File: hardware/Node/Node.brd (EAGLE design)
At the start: 49.5 x 49.5 mm, 71 parts, among them J1 AVR_SPI_PRG_6NS, J2 M04X2, Q1 PMR280UN, Q2 PMR280UN, Q3 PMR280UN, SW1 KSS, SW2 KSS, U1 ATMEGA32U4QFN, U2 BLUETOOTH-RN41", U3 LSM303DLM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

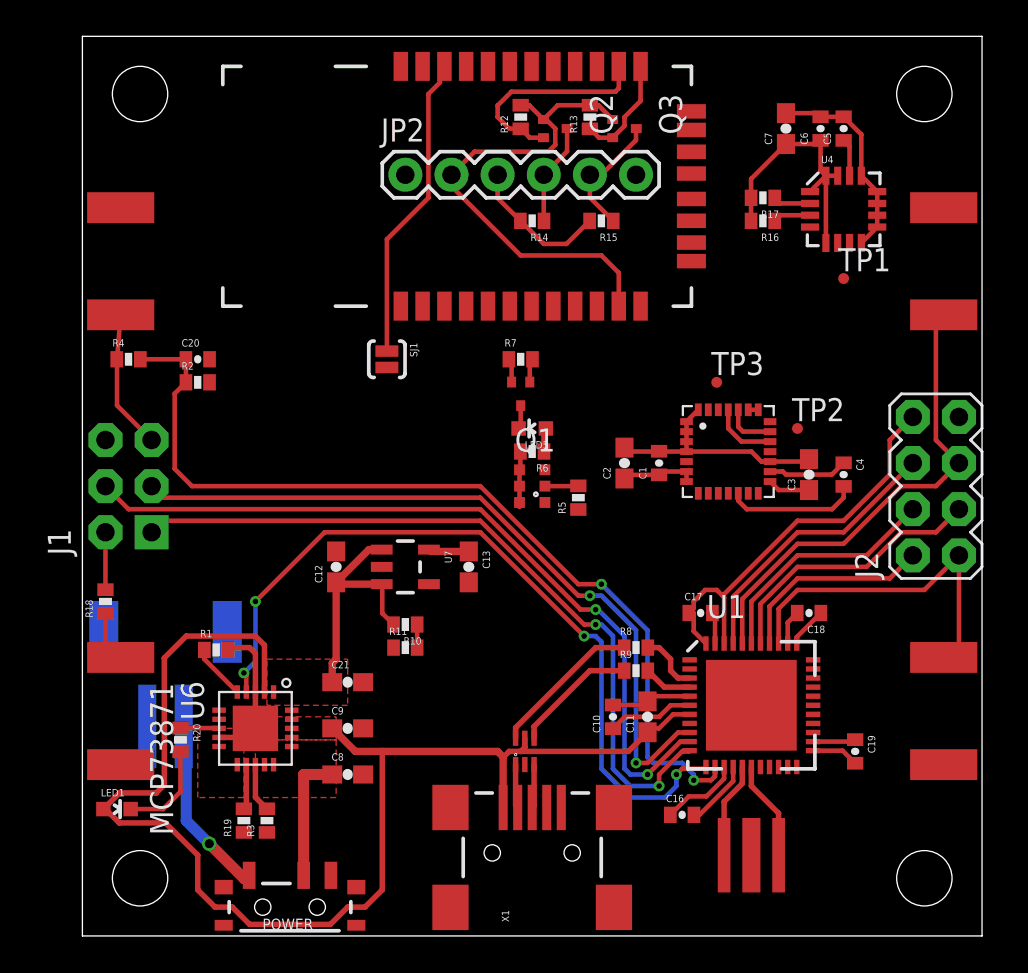
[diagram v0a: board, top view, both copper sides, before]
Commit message: route LEDs and interrupts
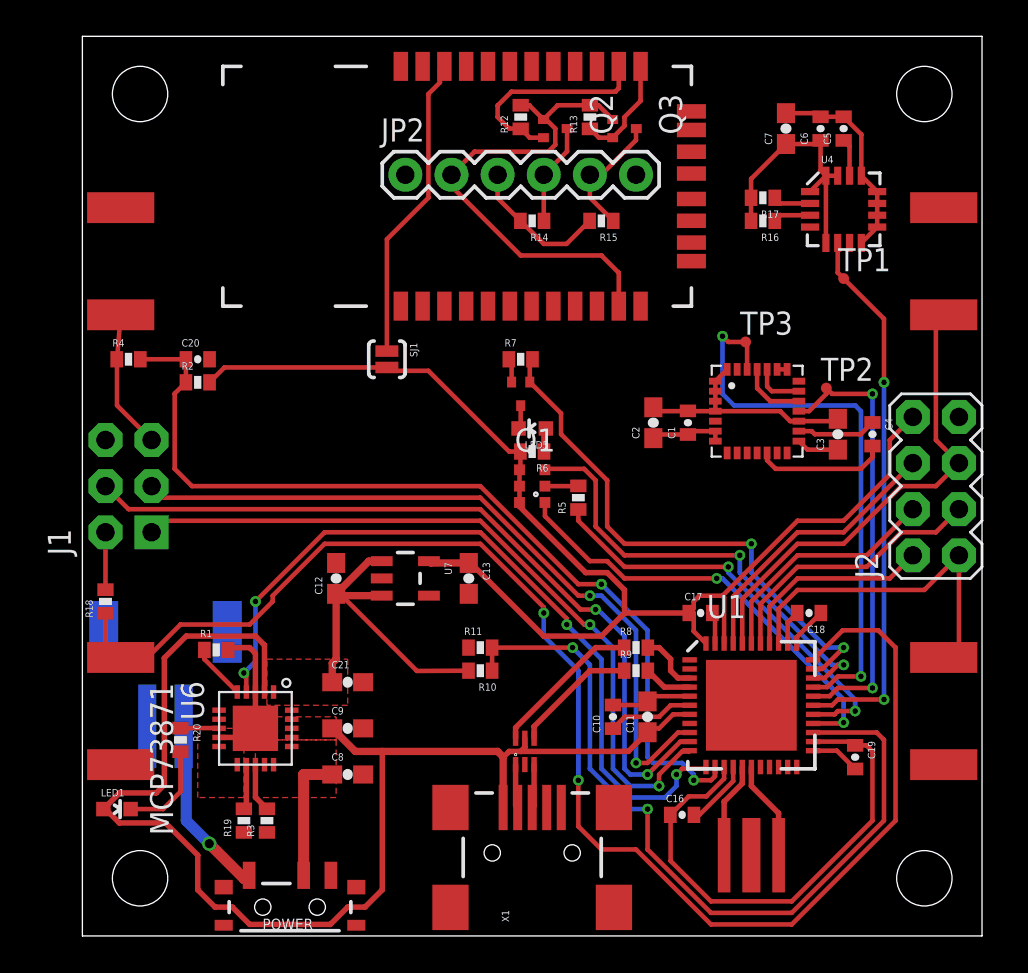
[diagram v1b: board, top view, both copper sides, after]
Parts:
- moved R10 4.85 mm to (21.9, 14.6)
- moved R11 4.13 mm to (21.9, 15.9)
- moved C4 2.73 mm to (43.5, 27.6)
- moved TP2 2.73 mm to (41.0, 30.2)
- moved TP3 2.73 mm to (36.5, 32.7)
- moved C2 2.73 mm to (31.4, 28.3)
- moved C1 2.73 mm to (33.3, 28.3)
- moved C3 2.73 mm to (41.6, 27.6)
- moved U3 2.73 mm to (37.1, 28.9)
- moved C12 0.64 mm to (14.0, 19.7)
- moved C13 0.64 mm to (21.3, 19.7)
- moved U7 0.64 mm to (17.8, 19.7)
- moved C19 0.32 mm to (42.5, 9.84)
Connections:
- net N$12: now also LED4.3; no longer LED4.1
- net N$17: now also LED4.1, U1.26; no longer LED4.3, U1.32
- net N$22: now also U1.32; no longer U1.26
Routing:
- net HWB: track 2.79 -> 80.4 mm, vias 0 -> 2
- net +3V3: track 92.7 -> 156.3 mm
- net VDIV: track 1.27 -> 44.2 mm, vias 0 -> 2
- net PCINT6: track 0.00 -> 31.6 mm, vias 0 -> 2
- net PCINT4: track 0.00 -> 30.2 mm, vias 0 -> 2
- net N$22: track 1.32 -> 29.9 mm, vias 0 -> 2
- net N$12: track 0.00 -> 24.7 mm, vias 0 -> 2
- net PCINT5: track 0.00 -> 24.5 mm, vias 0 -> 2
- net N$17: track 0.00 -> 24.3 mm, vias 0 -> 2
- net N$18: track 0.00 -> 23.1 mm, vias 0 -> 2
- net N$11: track 13.6 -> 19.9 mm

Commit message: lay ground pours
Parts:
- moved C5 2.22 mm to (41.9, 42.2)
- moved C6 2.22 mm to (40.6, 42.2)
- moved C7 2.22 mm to (38.7, 42.2)
- moved R17 2.22 mm to (37.5, 38.4)
- moved TP1 2.22 mm to (41.9, 34.0)
- moved U4 2.22 mm to (41.9, 37.8)
- moved R16 2.22 mm to (37.5, 37.1)
- moved TP2 0.63 mm to (41.6, 30.2)
- moved TP3 0.32 mm to (36.2, 32.7)
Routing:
- net +3V3: track 156.3 -> 233.0 mm, vias 0 -> 8
- net RX: track 11.9 -> 69.3 mm, vias 0 -> 2
- net TX: track 6.02 -> 60.3 mm, vias 0 -> 2
- net SCL: track 4.89 -> 55.4 mm, vias 0 -> 2
- net SDA: track 5.70 -> 53.2 mm, vias 0 -> 2
- net RBT: track 0.00 -> 46.1 mm, vias 0 -> 2
- net SBT: track 0.00 -> 37.8 mm, vias 0 -> 4
- net VBUS: track 72.0 -> 100.8 mm, vias 0 -> 2
- net GND: track 48.8 -> 44.6 mm
- net N$17: track 24.3 -> 28.2 mm
- net N$11: track 19.9 -> 18.2 mm
- net PROG2: track 42.5 -> 43.8 mm
- net PCINT4: track 30.2 -> 29.3 mm
- net N$18: track 23.1 -> 24.0 mm
- net MISO: track 41.0 -> 41.5 mm
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- added copper zone on layer 16, net GND

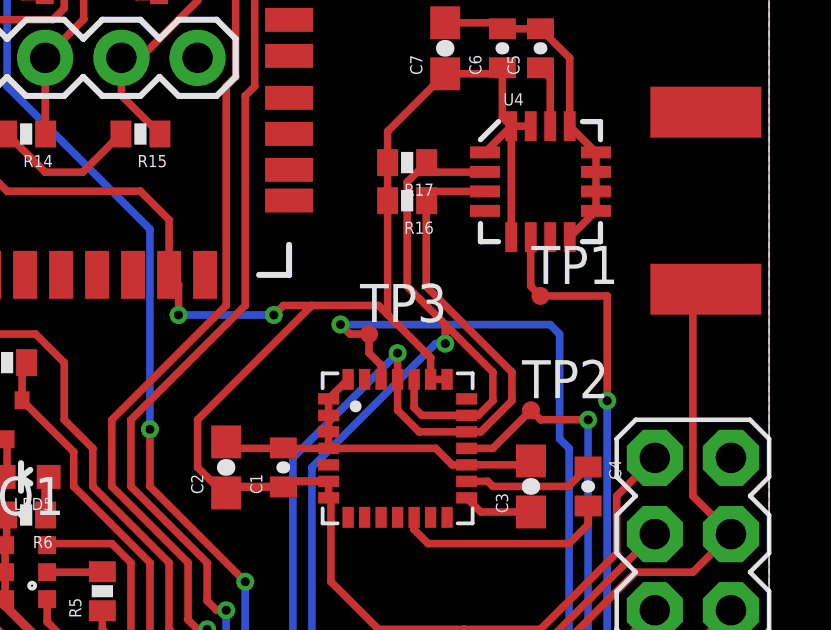
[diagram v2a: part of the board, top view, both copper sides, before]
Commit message: moved a trace to make the bottom fully connected
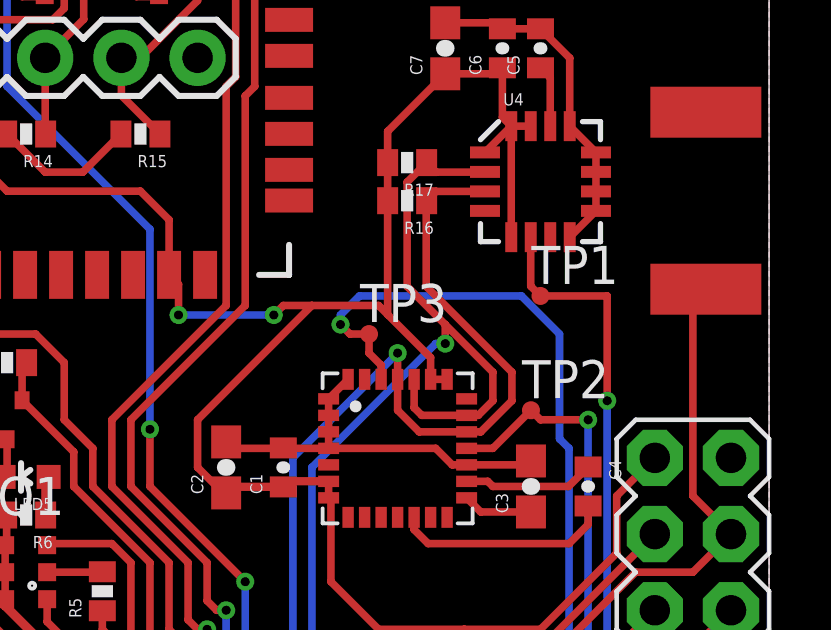
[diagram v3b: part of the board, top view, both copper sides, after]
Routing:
- net PCINT6: track 31.6 -> 32.6 mm
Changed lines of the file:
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@@
 <grid distance="0.05" unitdist="inch" unit="inch" style="dots" multiple="1" display="yes" altdistance="0.0125" altunitdist="inch" altunit="inch"/>
 <layers>
-<layer number="1" name="Top" color="4" fill="1" visible="yes" active="yes"/>
+<layer number="1" name="Top" color="4" fill="1" visible="no" active="yes"/>
 <layer number="16" name="Bottom" color="1" fill="1" visible="yes" active="yes"/>
 <layer number="17" name="Pads" color="2" fill="1" visible="yes" active="yes"/>
@@
 <wire x1="42.8625" y1="28.8925" x2="42.545" y2="29.21" width="0.254" layer="16"/>
 <wire x1="42.545" y1="29.21" x2="42.545" y2="32.7025" width="0.254" layer="16"/>
-<wire x1="42.545" y1="32.7025" x2="42.2275" y2="33.02" width="0.254" layer="16"/>
-<wire x1="42.2275" y1="33.02" x2="35.2425" y2="33.02" width="0.254" layer="16"/>
+<wire x1="42.545" y1="32.7025" x2="41.275" y2="33.9725" width="0.254" layer="16"/>
+<wire x1="41.275" y1="33.9725" x2="35.8775" y2="33.9725" width="0.254" layer="16"/>
+<wire x1="35.8775" y1="33.9725" x2="35.2425" y2="33.3375" width="0.254" layer="16"/>
+<wire x1="35.2425" y1="33.3375" x2="35.2425" y2="33.02" width="0.254" layer="16"/>
 <via x="35.2425" y="33.02" extent="1-16" drill="0.3"/>
 <wire x1="36.195" y1="32.7025" x2="35.56" y2="32.7025" width="0.254" layer="1"/>

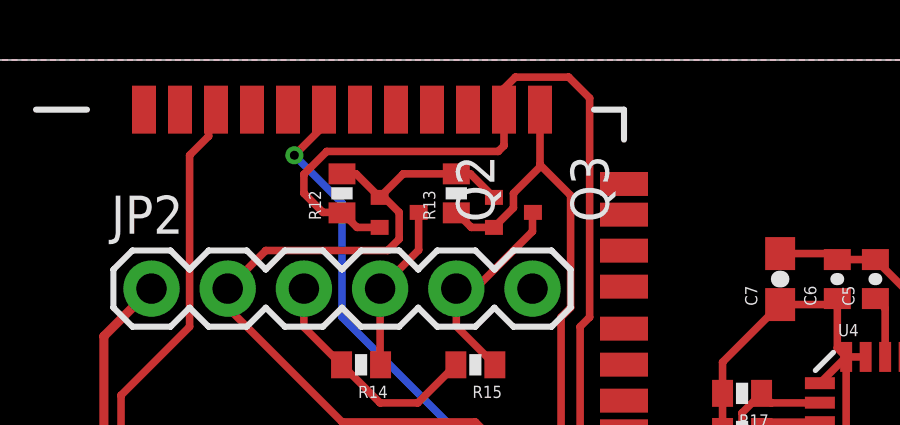
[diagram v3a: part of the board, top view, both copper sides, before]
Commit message: expand keepout to board edge, fix ground pours
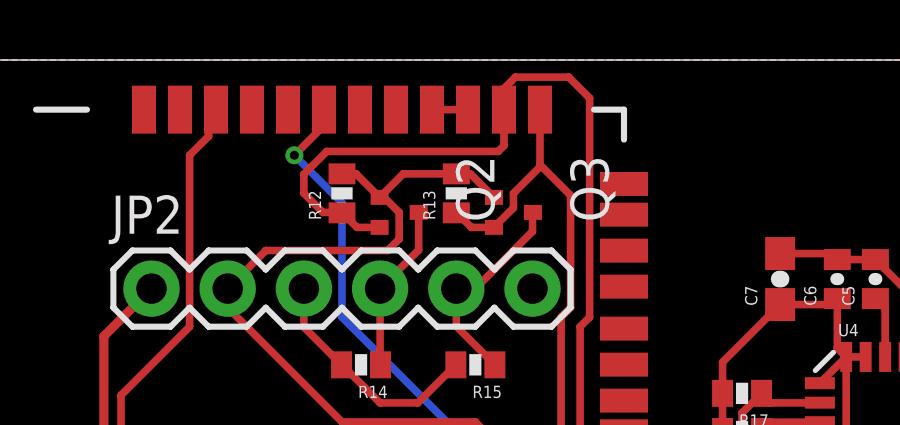
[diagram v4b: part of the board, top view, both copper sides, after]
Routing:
- net N$9: track 0.00 -> 1.20 mm
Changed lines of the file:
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@@
 <grid distance="0.05" unitdist="inch" unit="inch" style="dots" multiple="1" display="yes" altdistance="0.0125" altunitdist="inch" altunit="inch"/>
 <layers>
-<layer number="1" name="Top" color="4" fill="1" visible="no" active="yes"/>
+<layer number="1" name="Top" color="4" fill="1" visible="yes" active="yes"/>
 <layer number="16" name="Bottom" color="1" fill="1" visible="yes" active="yes"/>
 <layer number="17" name="Pads" color="2" fill="1" visible="yes" active="yes"/>
@@
 <wire x1="49.53" y1="49.53" x2="0" y2="49.53" width="0" layer="20"/>
 <wire x1="0" y1="49.53" x2="0" y2="0" width="0" layer="20"/>
-<rectangle x1="6.985" y1="34.29" x2="15.875" y2="48.26" layer="39"/>
-<rectangle x1="6.985" y1="34.29" x2="15.875" y2="48.26" layer="41"/>
-<rectangle x1="6.985" y1="34.29" x2="15.875" y2="48.26" layer="40"/>
-<rectangle x1="6.985" y1="34.29" x2="15.875" y2="48.26" layer="42"/>
+<rectangle x1="6.985" y1="34.29" x2="15.875" y2="49.53" layer="39"/>
+<rectangle x1="6.985" y1="34.29" x2="15.875" y2="49.53" layer="41"/>
+<rectangle x1="6.985" y1="34.29" x2="15.875" y2="49.53" layer="40"/>
+<rectangle x1="6.985" y1="34.29" x2="15.875" y2="49.53" layer="42"/>
 </plain>
 <attributes>
@@
 <vertex x="14.605" y="16.51"/>
 </polygon>
-<polygon width="0.254" layer="1" orphans="yes">
+<polygon width="0.254" layer="1" isolate="0.254" orphans="yes" rank="6">
 <vertex x="0" y="49.53"/>
 <vertex x="49.53" y="49.53"/>
@@
 <vertex x="0" y="0"/>
 </polygon>
-<polygon width="0.254" layer="16" orphans="yes">
+<polygon width="0.254" layer="16" isolate="0.254" orphans="yes" rank="6">
 <vertex x="0" y="49.53"/>
 <vertex x="49.53" y="49.53"/>
@@
 <vertex x="0" y="0"/>
 </polygon>
-<wire x1="2.1082" y1="9.4325" x2="3.572" y2="11.54" width="0" layer="19" extent="1-16"/>
-<wire x1="33.02" y1="44.45" x2="30.48" y2="41.91" width="0" layer="19" extent="1-1"/>
-<wire x1="40.06" y1="36.8075" x2="42.885" y2="35.9325" width="0" layer="19" extent="1-1"/>
-<wire x1="7.525" y1="10.93" x2="3.572" y2="11.54" width="0" layer="19" extent="1-16"/>
-<wire x1="15.455" y1="8.89" x2="15.455" y2="11.43" width="0" layer="19" extent="1-1"/>
-<wire x1="9.525" y1="13.43" x2="7.525" y2="10.93" width="0" layer="19" extent="1-1"/>
-<wire x1="16.4799" y1="19.685" x2="15.455" y2="13.97" width="0" layer="19" extent="1-1"/>
-<wire x1="24.3586" y1="9.4361" x2="21.2575" y2="15.875" width="0" layer="19" extent="1-1"/>
-<wire x1="26.365" y1="7.072" x2="24.3586" y2="9.4361" width="0" layer="19" extent="1-1"/>
-<wire x1="29.21" y1="12.715" x2="24.3586" y2="9.4361" width="0" layer="19" extent="1-1"/>
-<wire x1="34.83" y1="16.1" x2="33.43" y2="13.2" width="0" layer="19" extent="1-1"/>
-<wire x1="38.83" y1="16.1" x2="34.83" y2="16.1" width="0" layer="19" extent="1-1"/>
+<wire x1="34.83" y1="16.1" x2="38.83" y2="16.1" width="0" layer="19" extent="1-1"/>
+<wire x1="33.43" y1="13.2" x2="34.83" y2="16.1" width="0" layer="19" extent="1-1"/>
 <wire x1="35.83" y1="9.3" x2="33.43" y2="13.2" width="0" layer="19" extent="1-1"/>
 <wire x1="36.83" y1="4.445" x2="33.9725" y2="6.6675" width="0" layer="19" extent="1-1"/>
 <wire x1="40.23" y1="10.2" x2="35.83" y2="9.3" width="0" layer="19" extent="1-1"/>
 <wire x1="47.4218" y1="9.4325" x2="42.545" y2="9.1925" width="0" layer="19" extent="1-1"/>
+<wire x1="24.3586" y1="9.4361" x2="29.21" y2="12.715" width="0" layer="19" extent="1-1"/>
+<wire x1="26.365" y1="7.072" x2="24.3586" y2="9.4361" width="0" layer="19" extent="1-1"/>
+<wire x1="21.2575" y1="15.875" x2="24.3586" y2="9.4361" width="0" layer="19" extent="1-1"/>
+<wire x1="15.455" y1="13.97" x2="16.4799" y2="19.685" width="0" layer="19" extent="1-1"/>
+<wire x1="15.455" y1="8.89" x2="15.455" y2="11.43" width="0" layer="19" extent="1-1"/>
+<wire x1="9.525" y1="13.43" x2="15.455" y2="13.97" width="0" layer="19" extent="1-1"/>
+<wire x1="7.525" y1="10.93" x2="9.525" y2="13.43" width="0" layer="19" extent="1-1"/>
+<wire x1="3.572" y1="11.54" x2="7.525" y2="10.93" width="0" layer="19" extent="1-16"/>
+<wire x1="2.1082" y1="9.4325" x2="3.572" y2="11.54" width="0" layer="19" extent="1-16"/>
+<wire x1="33.02" y1="44.45" x2="30.48" y2="41.91" width="0" layer="19" extent="1-1"/>
+<wire x1="40.06" y1="36.8075" x2="42.885" y2="35.9325" width="0" layer="19" extent="1-1"/>
 <wire x1="7" y1="31.75" x2="1.27" y2="27.305" width="0" layer="19" extent="1-1"/>
 <wire x1="23.63" y1="31.6" x2="30.73" y2="34.675" width="0" layer="19" extent="1-1"/>
+<wire x1="22.33" y1="47.875" x2="30.48" y2="41.91" width="0" layer="19" extent="1-1"/>
 </signal>
 <signal name="+3V3">
@@
 <via x="12.7" y="19.685" extent="1-16" drill="0.5"/>
 <wire x1="12.7" y1="19.685" x2="9.525" y2="16.51" width="0.3048" layer="1"/>
-<wire x1="11.525" y1="11.93" x2="11.525" y2="11.43" width="0" layer="19" extent="1-1"/>
-<wire x1="11.525" y1="10.93" x2="11.525" y2="11.43" width="0" layer="19" extent="1-1"/>
-<wire x1="10.025" y1="13.43" x2="11.525" y2="11.93" width="0" layer="19" extent="1-1"/>
 <wire x1="1.27" y1="6.985" x2="1.155" y2="6.985" width="0" layer="19" extent="1-1"/>
 </signal>
@@
 <contactref element="U2" pad="15"/>
 <contactref element="U2" pad="16"/>
-<wire x1="27.13" y1="47.875" x2="28.33" y2="47.875" width="0" layer="19" extent="1-1"/>
+<wire x1="28.33" y1="47.875" x2="27.13" y2="47.875" width="0.254" layer="1"/>
 </signal>
 <signal name="N$18">
@@
 <wire x1="12.18" y1="3.3375" x2="12.18" y2="8.89" width="0.6096" layer="1"/>
 <wire x1="12.18" y1="8.89" x2="13.755" y2="8.89" width="0.6096" layer="1"/>
-<wire x1="10.525" y1="9.43" x2="11.525" y2="10.43" width="0" layer="19" extent="1-1"/>
-<wire x1="10.025" y1="9.43" x2="10.525" y2="9.43" width="0" layer="19" extent="1-1"/>
-<wire x1="12.18" y1="8.89" x2="11.525" y2="10.43" width="0" layer="19" extent="1-1"/>
 </signal>
 <signal name="N$8">
@@
 <wire x1="17.145" y1="14.59" x2="16.8125" y2="14.9225" width="0.3048" layer="1"/>
 <wire x1="16.8125" y1="14.9225" x2="13.97" y2="14.9225" width="0.3048" layer="1"/>
-<wire x1="13.97" y1="14.9225" x2="13.755" y2="15.025" width="0" layer="19" extent="1-1"/>
-<wire x1="11.525" y1="12.43" x2="13.755" y2="13.97" width="0" layer="19" extent="1-1"/>
 <wire x1="10.525" y1="13.43" x2="11.525" y2="12.43" width="0" layer="19" extent="1-1"/>
 </signal>

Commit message: added vias, 1 airwire left!!!
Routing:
- net GND: track 44.6 -> 57.1 mm, vias 0 -> 68
- net N$11: track 18.2 -> 20.1 mm
- net N$29: track 8.66 -> 10.1 mm
- net +3V3: track 233.0 -> 234.1 mm

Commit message: Ratsnest: Nothing to do!
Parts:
- moved U9 0.63 mm to (24.4, 10.8)
- moved C10 0.32 mm to (29.2, 12.4)
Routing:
- net GND: track 57.1 -> 59.3 mm, vias 68 -> 70
- net D+: track 2.41 -> 3.36 mm
- net D-: track 2.41 -> 3.34 mm
